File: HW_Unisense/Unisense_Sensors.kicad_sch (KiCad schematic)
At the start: 19 parts, among them U1 PCF85263ATT, U13 ZMOD4510AI1R, U4 TMP112xxDRL, U5 BME280, U6 BMP280, U7 VEML6040A3OG, Y1 Crystal

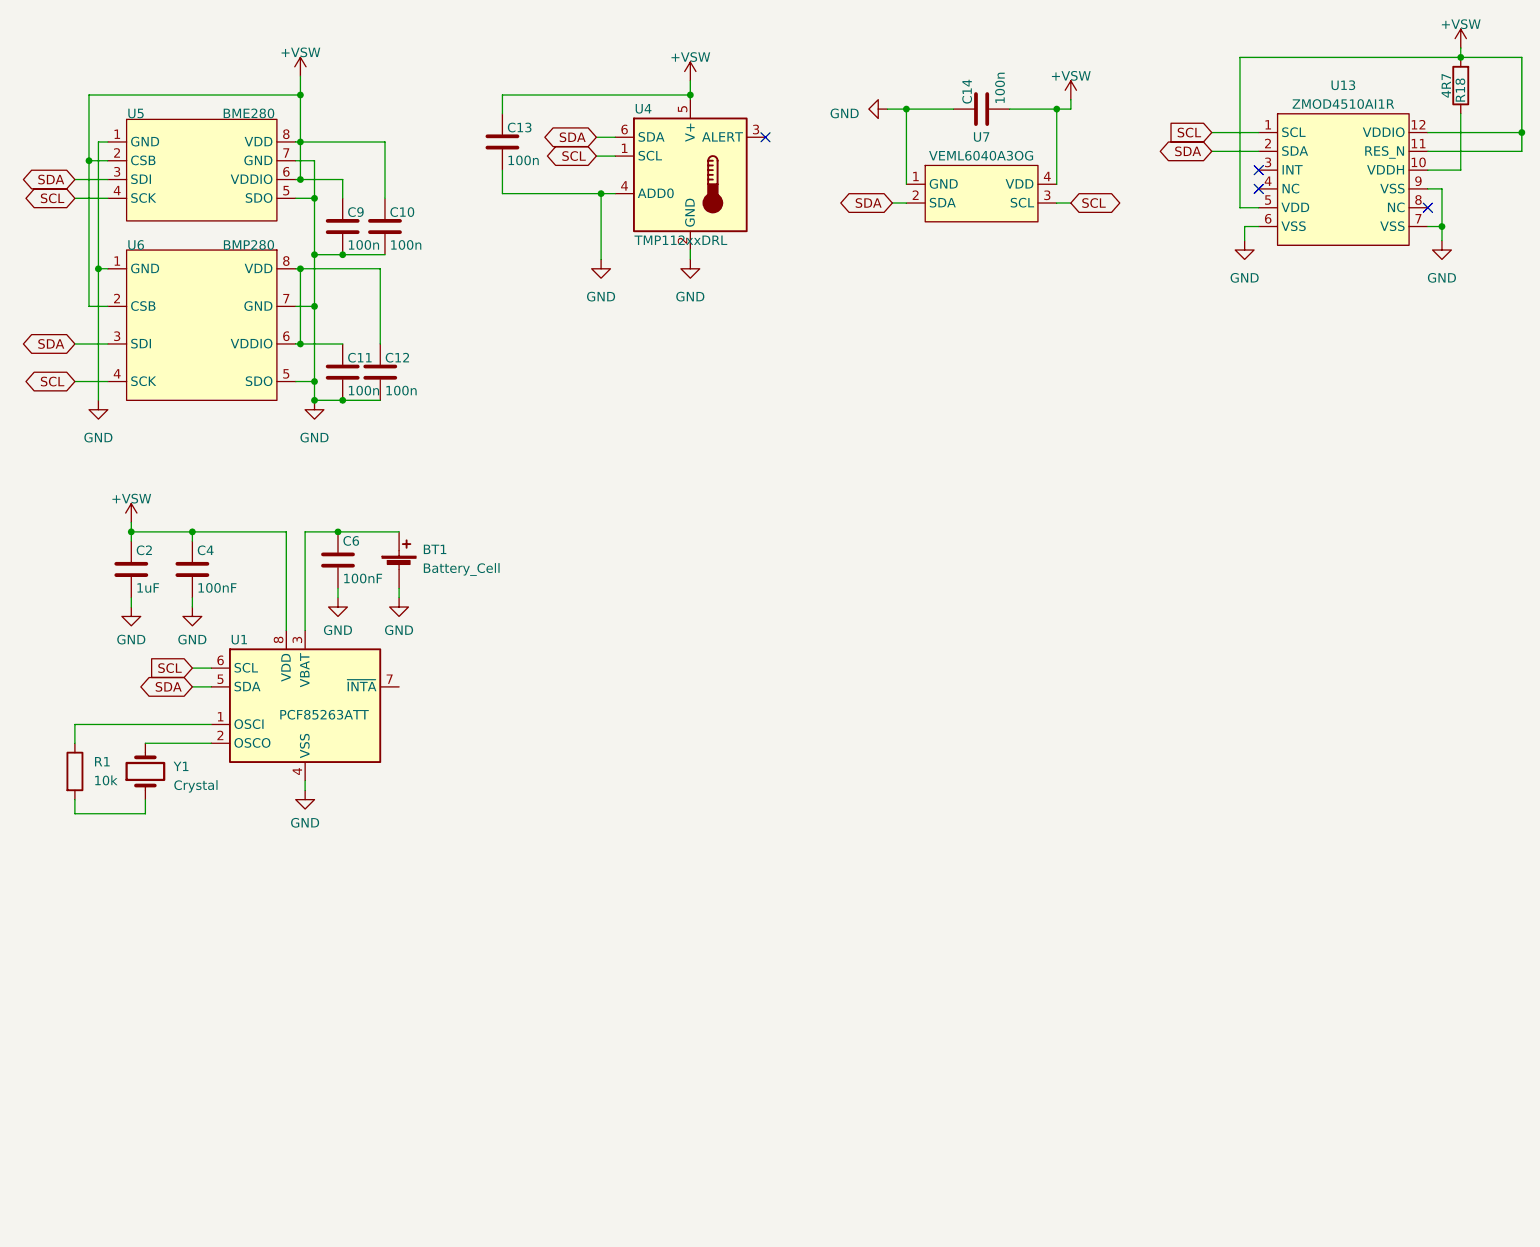
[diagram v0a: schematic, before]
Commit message: change power net names, as V8 handles them like a champ
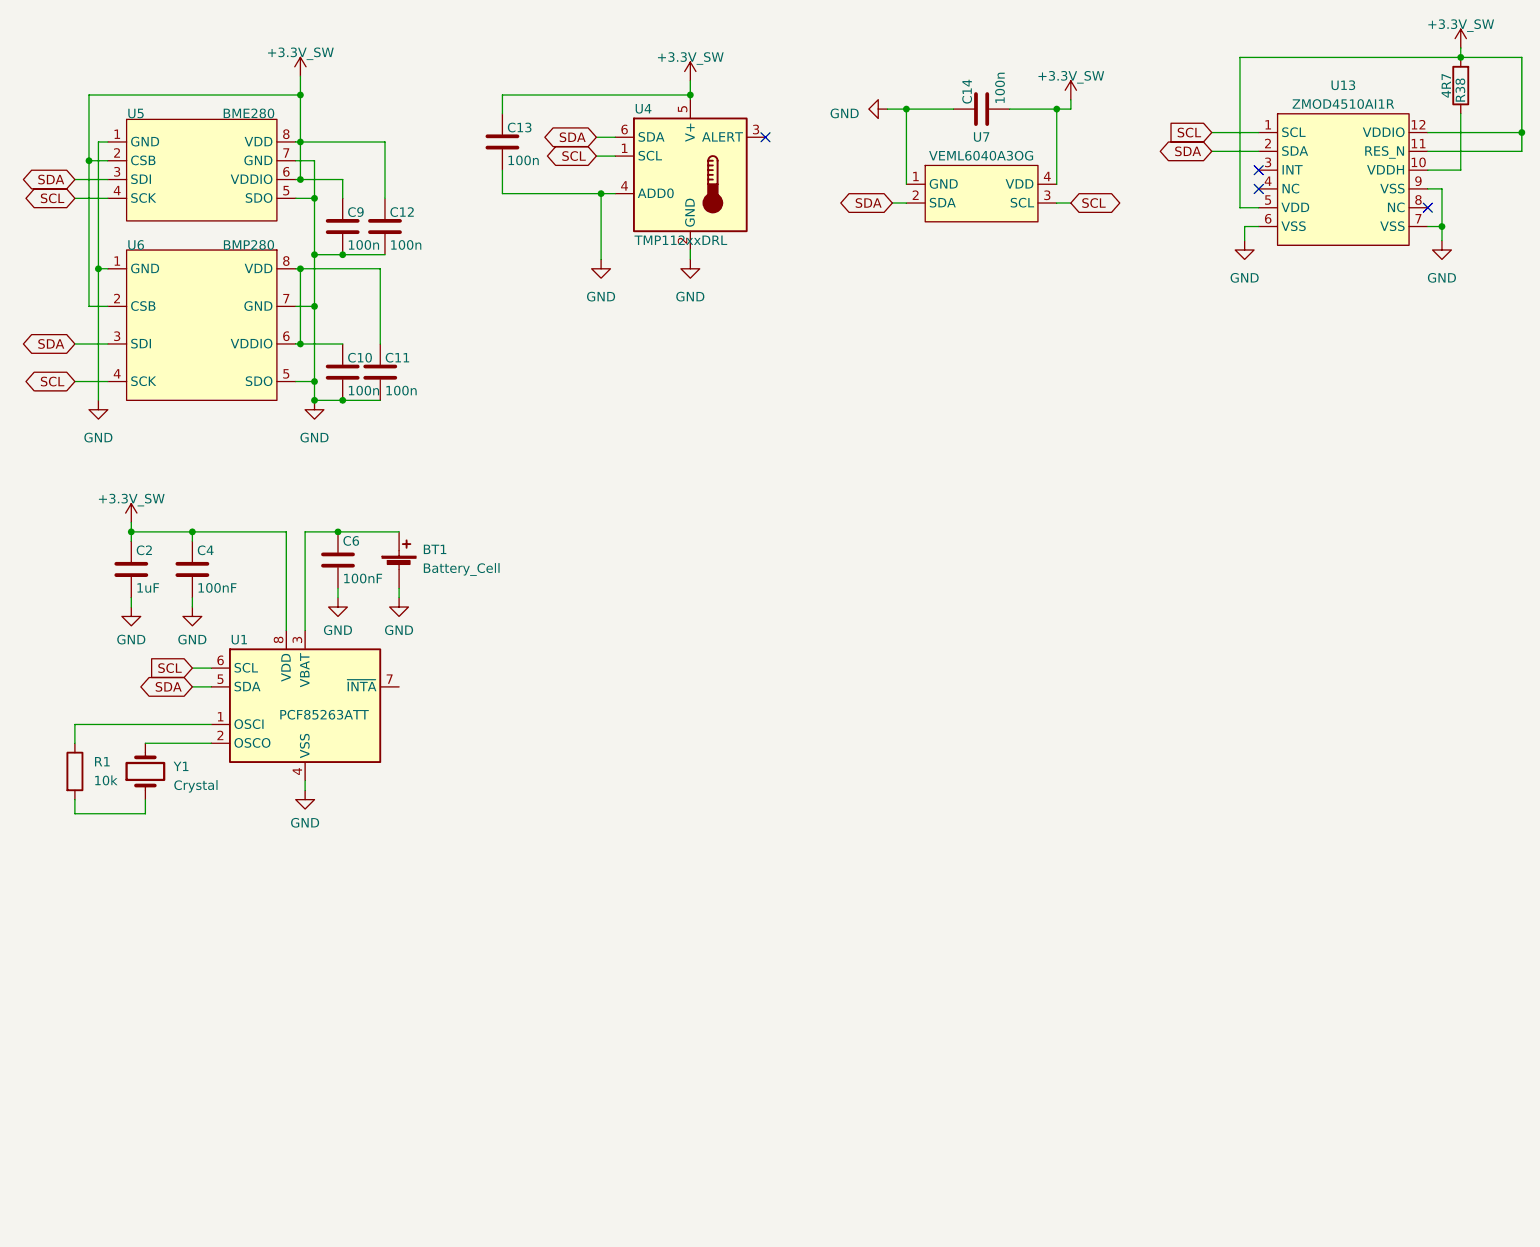
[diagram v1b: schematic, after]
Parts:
- renumbered C11 to C10, C12 to C11, C10 to C12, R18 to R38
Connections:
- net +VSW renamed +3.3V_SW

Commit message: add mor sensors, place parts
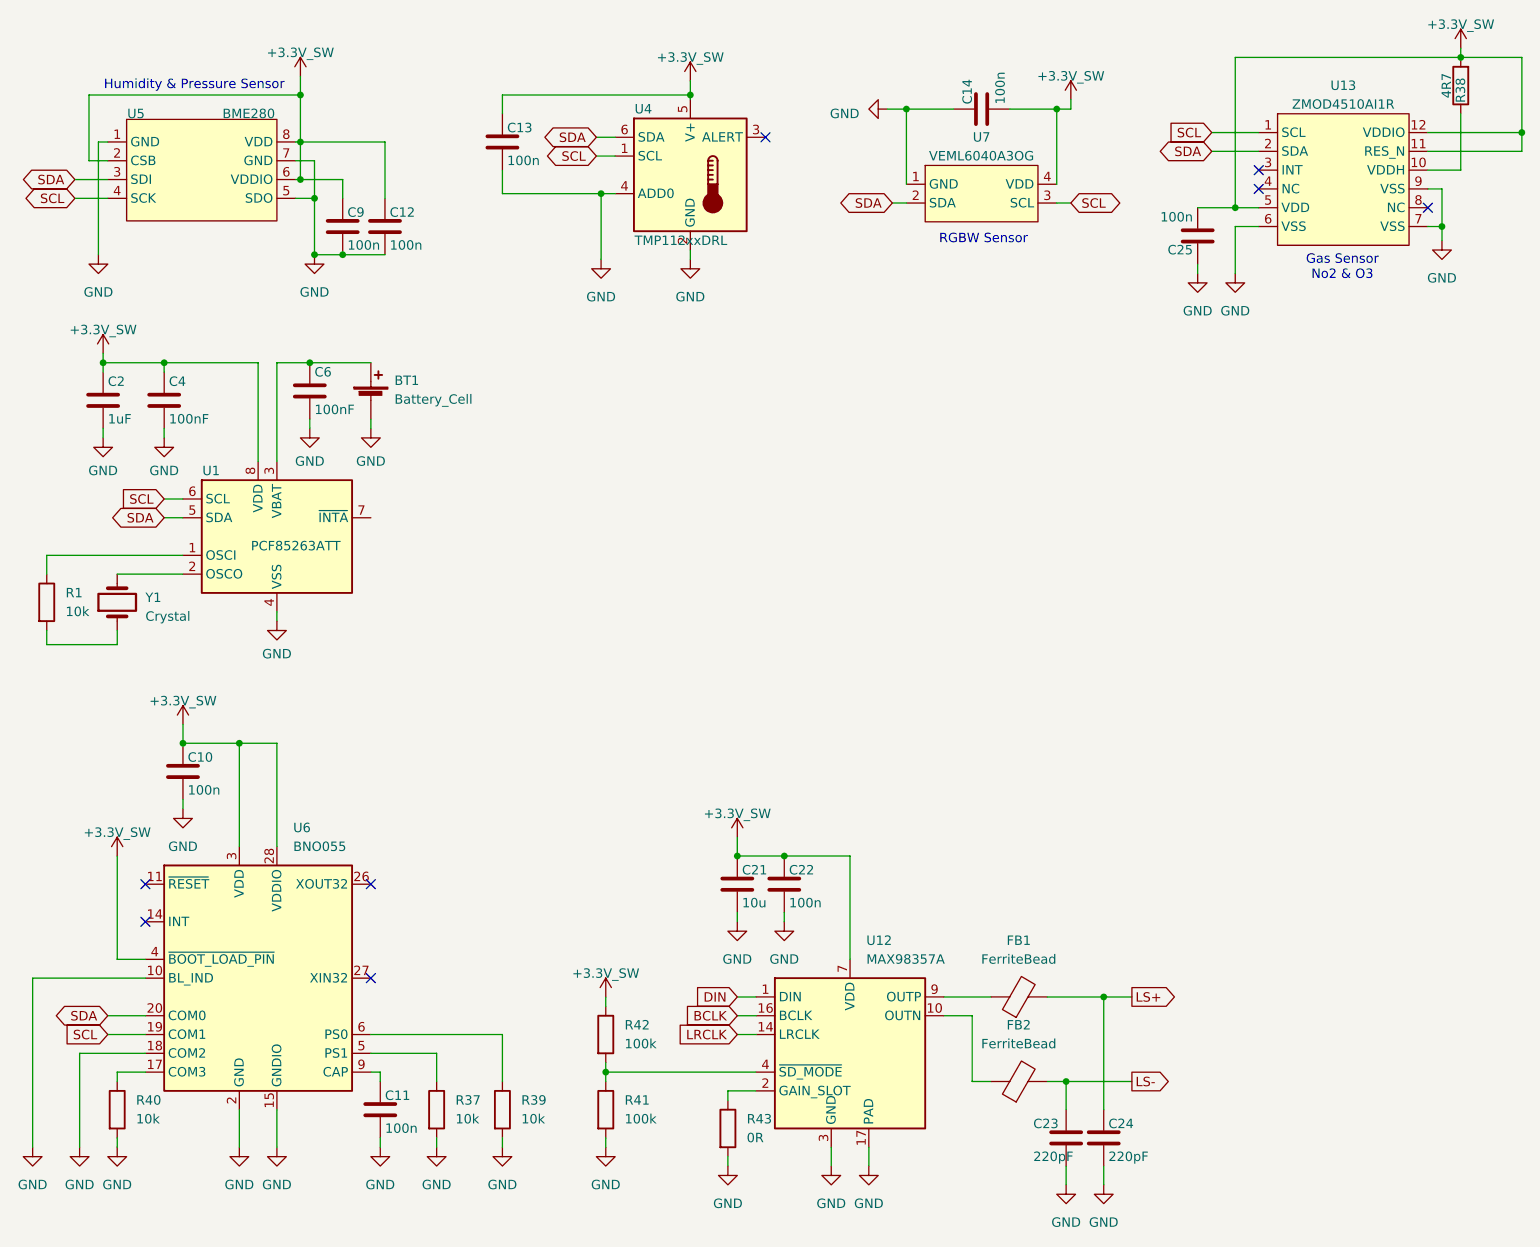
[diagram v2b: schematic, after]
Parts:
- removed U6: BMP280, burgerLibFP:LGA-8_L2.5-W2.0-P0.65_AMP6127, symbol burgerLib:BMP280
- added C21: 10u, Capacitor_SMD:C_0805_2012Metric, symbol Device:C
- added C22, C25: 100n, Capacitor_SMD:C_0603_1608Metric, symbol Device:C
- added C23, C24: 220pF, Capacitor_SMD:C_0603_1608Metric, symbol Device:C
- added FB1, FB2: FerriteBead, Inductor_SMD:L_0805_2012Metric_Pad1.15x1.40mm_HandSolder, symbol Device:FerriteBead
- added R37, R39, R40: 10k, Resistor_SMD:R_0603_1608Metric_Pad0.98x0.95mm_HandSolder, symbol Device:R
- added R41, R42: 100k, Resistor_SMD:R_0603_1608Metric_Pad0.98x0.95mm_HandSolder, symbol Device:R
- added R43: 0R, Resistor_SMD:R_0805_2012Metric_Pad1.20x1.40mm_HandSolder, symbol Device:R
- added U12: MAX98357A, Package_DFN_QFN:TQFN-16-1EP_3x3mm_P0.5mm_EP1.23x1.23mm, symbol Audio:MAX98357A
- added U6: BNO055, Package_LGA:LGA-28_5.2x3.8mm_P0.5mm, symbol Sensor_Motion:BNO055
- BT1: footprint JLCPCB:BAT-SMD_MYOUNG_MY-2032-04 -> burgerLibFP:BAT-SMD_MYOUNG_MY-2032-04
- R1: footprint Resistor_SMD:R_0805_2012Metric -> Resistor_SMD:R_0603_1608Metric_Pad0.98x0.95mm_HandSolder
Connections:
- net +3.3V_SW: now also C10.1, C21.1, C22.1, C25.2, R42.1, U12.7 (VDD), U12.8 (VDD), U6.28 (VDDIO), U6.3 (VDD), U6.4 (~{BOOT_LOAD_PIN})
- net GND: now also C21.2, C22.2, C23.2, C24.2, C25.1, R37.2, R39.2, R40.2, R41.2, R43.2, U12.11 (GND), U12.15 (GND), U12.17 (PAD), U12.3 (GND), U6.10 (BL_IND), U6.15 (GNDIO), U6.16 (GNDIO), U6.18 (COM2), U6.2 (GND), U6.25 (GNDIO)
- net SCL: now also U6.19 (COM1)
- net SDA: now also U6.20 (COM0)
- net at C11.1: now also U6.9 (CAP); no longer C10.1
- new net: R41.1, R42.2, U12.4 (~{SD_MODE})
- new net: R43.1, U12.2 (GAIN_SLOT)
- new net: R37.1, U6.5 (PS1)
- new net: R40.1, U6.17 (COM3)
- new net: R39.1, U6.6 (PS0)
- new net: FB2.1, U12.10 (OUTN)
- new net: FB1.1, U12.9 (OUTP)
- new net BCLK: U12.16 (BCLK)
- new net DIN: U12.1 (DIN)
- new net LRCLK: U12.14 (LRCLK)
- new net LS+: C24.1, FB1.2
- new net LS-: C23.1, FB2.2
- no-connect marks 4 -> 8
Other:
- note added: "Gas Sensor No2 & O3"
- note added: "Humidity & Pressure Sensor"
- note added: "RGBW Sensor"
- moved on the sheet: BT1, C2, C4, C6, R1, U1, Y1
